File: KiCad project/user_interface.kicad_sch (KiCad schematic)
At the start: 12 parts, among them J4 Conn_01x05, J6 B4B-XH-AM__LF__SN_, Q2 BC817, Q3 BC817, SW1 SMD_6x3.5mm_h2.5mm, SW2 SMD_6x3.5mm_h2.5mm

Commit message: Fixed lots of bugs.
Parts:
- removed R36: 10K, Resistor_SMD:R_0201_0603Metric, symbol Device:R
- C21: footprint SparkFun-Capacitor:C_0603_1608Metric -> Capacitor_SMD:C_0805_2012Metric
- C22: value 0.1u -> 1u; footprint SparkFun-Capacitor:C_0603_1608Metric -> Capacitor_SMD:C_0805_2012Metric; Purpose Debounce capacitor -> (none)
- J5: renamed from J6; footprint B4B-XH-AM__LF__SN_:JST_B4B-XH-AM__LF__SN_ -> Project_Library:JST_B4B-XH-AM__LF__SN_
- J6: renamed from J4; footprint (none) -> Connector_PinHeader_2.54mm:PinHeader_1x05_P2.54mm_Vertical
- R32: renamed from R37; footprint Resistor_SMD:R_0201_0603Metric -> Resistor_SMD:R_0805_2012Metric
- R33: renamed from R13; footprint Resistor_SMD:R_0201_0603Metric -> Resistor_SMD:R_0805_2012Metric
- R34: renamed from R38; footprint Resistor_SMD:R_0201_0603Metric -> Resistor_SMD:R_0805_2012Metric
- SW1, SW2: footprint SparkFun-Switch:Push_SMD_6x3.5mm -> Button_Switch_THT:SW_PUSH_6mm

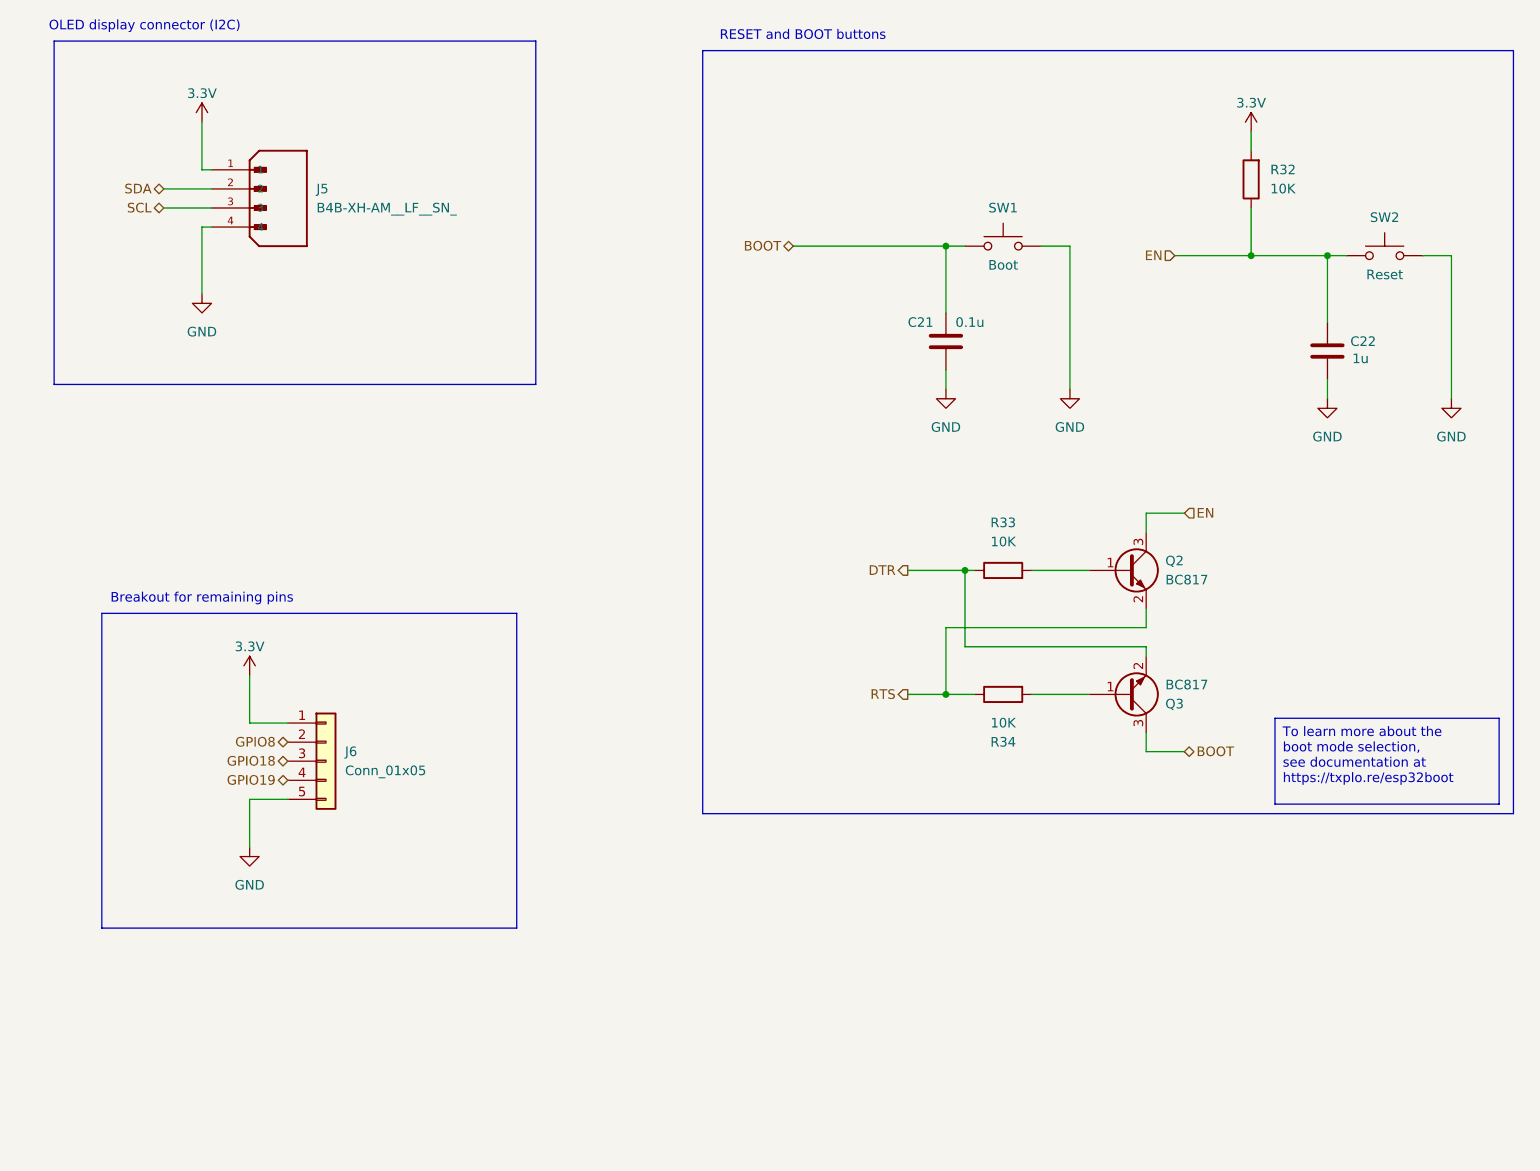
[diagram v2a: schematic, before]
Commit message: Replaced the button, USB, bat connector with new symbols and footprints. Completed draft layout and routing.
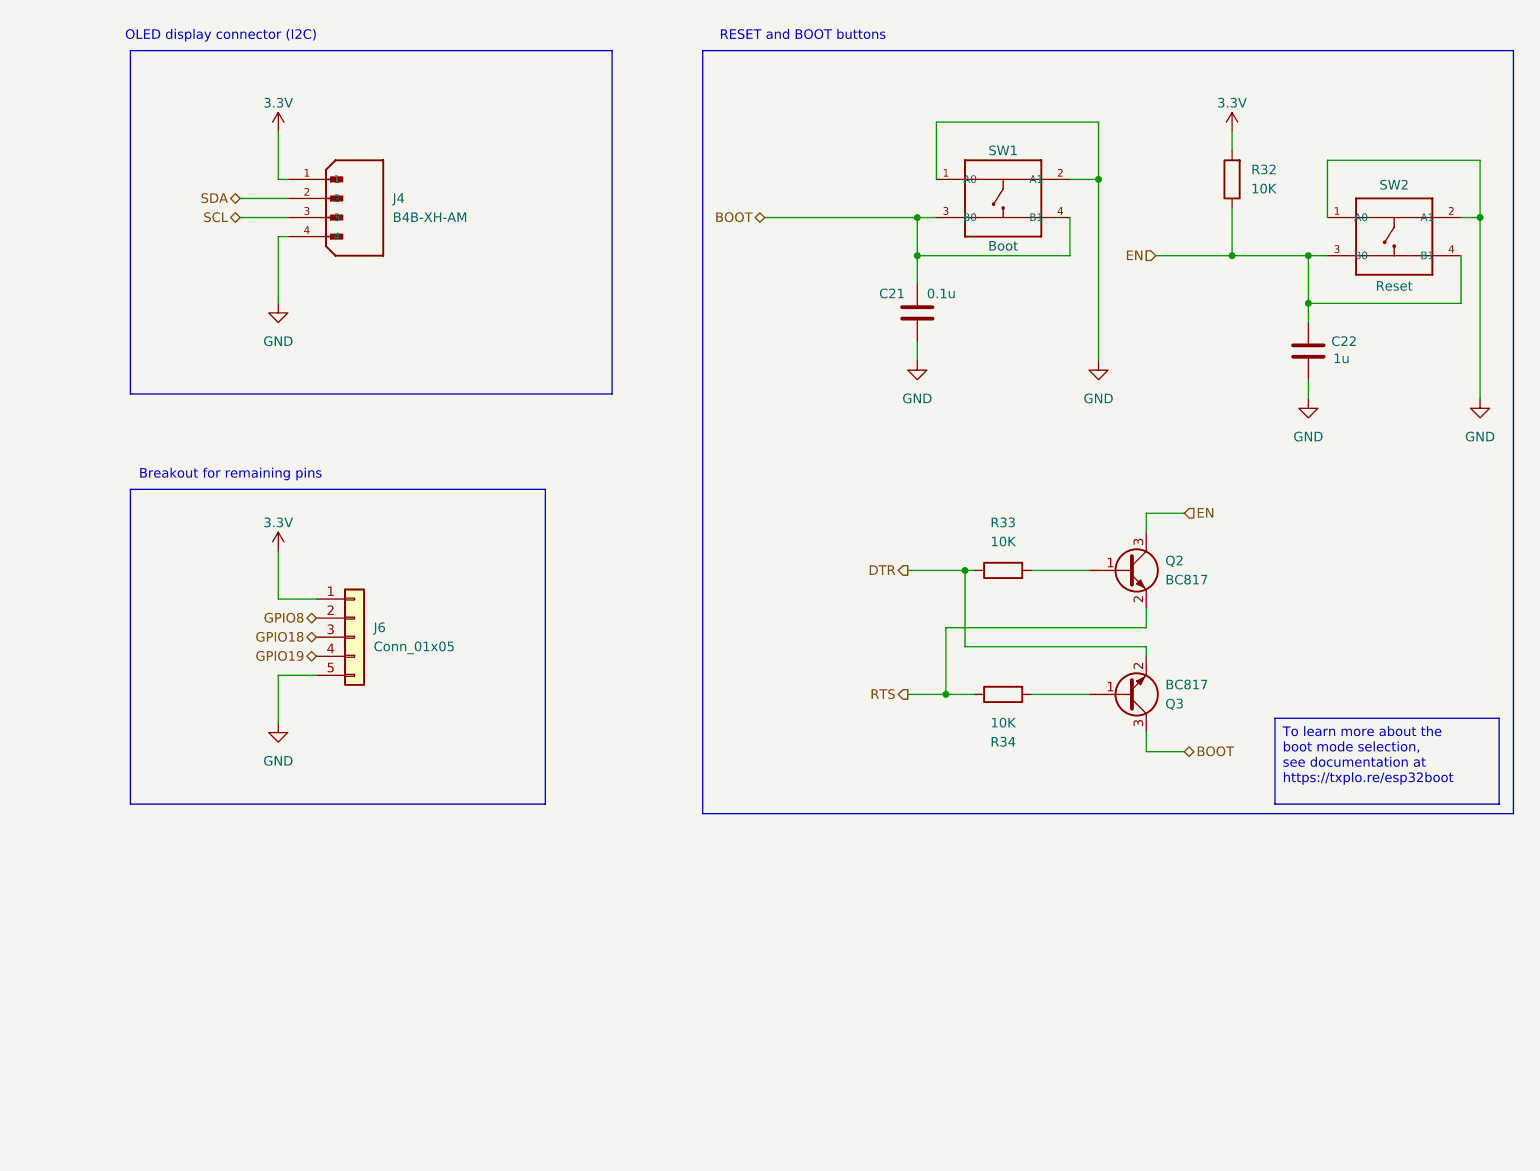
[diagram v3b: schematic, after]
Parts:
- J4: renamed from J5; value B4B-XH-AM__LF__SN_ -> B4B-XH-AM; Manufacturer_Part_Number (none) -> B4B-XH-AM
- Q2, Q3: Manufacturer_Part_Number (none) -> BC817; PACKAGE (none) -> SOT-23
- R32, R33, R34: PACKAGE (none) -> 0805
- SW1, SW2: value SMD_6x3.5mm_h2.5mm -> 1101NE; footprint Button_Switch_THT:SW_PUSH_6mm -> Footprints:SW4-SMD-5.2X5.2X1.5MM; symbol SparkFun-Switch:SPST_Push_SMD_6x3.5mm_h2.5mm -> SMD-BUTTON_4P-5.2X5.2X1.5MM-SKQGADE010_:SMD-BUTTON_4P-5.2X5.2X1.5MM-SKQGADE010_; Availability (none) -> In Stock; Check_prices (none) -> https://www.snapeda.com/parts/SKQGADE010/ALPS/view-part/?re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; Description_1 (none) -> Switch Tactile N.O. SPST Round Button Gull Wing 0.05A 12VDC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; MF (none) -> ALPS; MP (none) -> SKQGADE010; Manufacturer_Part_Number (none) -> 1101NE; Package (none) -> SMD-4 ALPS; Price (none) -> None; SnapEDA_Link (none) -> https://www.snapeda.com/parts/SKQGADE010/ALPS/view-part/?re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
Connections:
- net BOOT: now also SW1.3 (B0), SW1.4 (B1); no longer SW1.1
- net EN: now also SW2.3 (B0), SW2.4 (B1); no longer SW2.1
- net GND: now also SW1.1 (A0), SW2.1 (A0)
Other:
- moved on the sheet: C21, C22, J4, J6, R32

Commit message: Completed draft of the layout.
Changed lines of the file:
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@@
+	)
+	(symbol
+		(lib_id "Graphic:Logo_Open_Hardware_Small")
+		(at 52.07 185.42 0)
+		(unit 1)
+		(exclude_from_sim yes)
+		(in_bom no)
+		(on_board yes)
+		(dnp no)
+		(fields_autoplaced yes)
+		(property "Reference" "#SYM3"
+			(at 52.07 178.435 0)
+			(effects
+				(font
+					(size 1.27 1.27)
+				)
+				(hide yes)
+			)
+		)
+		(property "Value" "Logo_Open_Hardware_Small"
+			(at 52.07 191.135 0)
+			(effects
+				(font
+					(size 1.27 1.27)
+				)
+				(hide yes)
+			)
+		)
+		(property "Footprint" "Footprints:TE_Logo_11.6x4"
+			(at 52.07 185.42 0)
+			(effects
+				(font
+					(size 1.27 1.27)
+				)
+				(hide yes)
+			)
+		)
+		(property "Datasheet" "~"
+			(at 52.07 185.42 0)
+			(effects
+				(font
+					(size 1.27 1.27)
+				)
+				(hide yes)
+			)
+		)
+		(property "Description" "Open Hardware logo, small"
+			(at 52.07 185.42 0)
+			(effects
+				(font
+					(size 1.27 1.27)
+				)
+				(hide yes)
+			)
+		)
+		(property "Comments" ""
+			(at 52.07 185.42 0)
+			(effects
+				(font
+					(size 1.27 1.27)
+				)
+				(hide yes)
+			)
+		)
+		(instances
+			(project "ESP32 sensor board"
+				(path "/16c571a0-8550-4f05-972c-22b0701cbf02/09ec4a32-ddff-43cd-8e21-9ef822101853/9638f799-907f-4116-a2c8-fb3f1731f620"
+					(reference "#SYM3")
+					(unit 1)
+				)
+			)
+		)
 	)
 	(symbol
@@
 	)
 	(symbol
+		(lib_id "Graphic:Logo_Open_Hardware_Small")
+		(at 52.07 171.45 0)
+		(unit 1)
+		(exclude_from_sim yes)
+		(in_bom no)
+		(on_board yes)
+		(dnp no)
+		(fields_autoplaced yes)
+		(property "Reference" "#SYM2"
+			(at 52.07 164.465 0)
+			(effects
+				(font
+					(size 1.27 1.27)
+				)
+				(hide yes)
+			)
+		)
+		(property "Value" "Logo_Open_Hardware_Small"
+			(at 52.07 177.165 0)
+			(effects
+				(font
+					(size 1.27 1.27)
+				)
+				(hide yes)
+			)
+		)
+		(property "Footprint" "Symbol:KiCad-Logo_5mm_SilkScreen"
+			(at 52.07 171.45 0)
+			(effects
+				(font
+					(size 1.27 1.27)
+				)
+				(hide yes)
+			)
+		)
+		(property "Datasheet" "~"
+			(at 52.07 171.45 0)
+			(effects
+				(font
+					(size 1.27 1.27)
+				)
+				(hide yes)
+			)
+		)
+		(property "Description" "Open Hardware logo, small"
+			(at 52.07 171.45 0)
+			(effects
+				(font
+					(size 1.27 1.27)
+				)
+				(hide yes)
+			)
+		)
+		(property "Comments" ""
+			(at 52.07 171.45 0)
+			(effects
+				(font
+					(size 1.27 1.27)
+				)
+				(hide yes)
+			)
+		)
+		(instances
+			(project "ESP32 sensor board"
+				(path "/16c571a0-8550-4f05-972c-22b0701cbf02/09ec4a32-ddff-43cd-8e21-9ef822101853/9638f799-907f-4116-a2c8-fb3f1731f620"
+					(reference "#SYM2")
+					(unit 1)
+				)
+			)
+		)
+	)
+	(symbol
 		(lib_id "Transistor_BJT:BC817")
 		(at 179.07 128.27 0)
@@
 					(unit 1)
 				)
+			)
+		)
+	)
+	(symbol
+		(lib_id "Graphic:Logo_Open_Hardware_Small")
+		(at 52.07 157.48 0)
+		(unit 1)
+		(exclude_from_sim no)
+		(in_bom no)
+		(on_board yes)
+		(dnp no)
+		(fields_autoplaced yes)
+		(property "Reference" "#SYM1"
+			(at 52.07 150.495 0)
+			(effects
+				(font
+					(size 1.27 1.27)
+				)
+				(hide yes)
+			)
+		)
+		(property "Value" "Logo_Open_Hardware_Small"
+			(at 52.07 163.195 0)
+			(effects
+				(font
+					(size 1.27 1.27)
+				)
+				(hide yes)
+			)
+		)
+		(property "Footprint" "Symbol:OSHW-Logo_5.7x6mm_SilkScreen"
+			(at 52.07 157.48 0)
+			(effects
+				(font
+					(size 1.27 1.27)
+				)
+				(hide yes)
+			)
+		)
+		(property "Datasheet" "~"
+			(at 52.07 157.48 0)
+			(effects
+				(font
+					(size 1.27 1.27)
+				)
+				(hide yes)
+			)
+		)
+		(property "Description" "Open Hardware logo, small"
+			(at 52.07 157.48 0)
+			(effects
+				(font
+					(size 1.27 1.27)
+				)
+				(hide yes)
+			)
+		)
+		(property "Sim.Enable" "0"
+			(at 52.07 157.48 0)
+			(effects
+				(font
+					(size 1.27 1.27)
+				)
+				(hide yes)
+			)
+		)
+		(property "Comments" ""
+			(at 52.07 157.48 0)
+			(effects
+				(font
+					(size 1.27 1.27)
+				)
+				(hide yes)
+			)
+		)
+		(instances
+			(project ""
+				(path "/16c571a0-8550-4f05-972c-22b0701cbf02/09ec4a32-ddff-43cd-8e21-9ef822101853/9638f799-907f-4116-a2c8-fb3f1731f620"
+					(reference "#SYM1")
+					(unit 1)
+				)

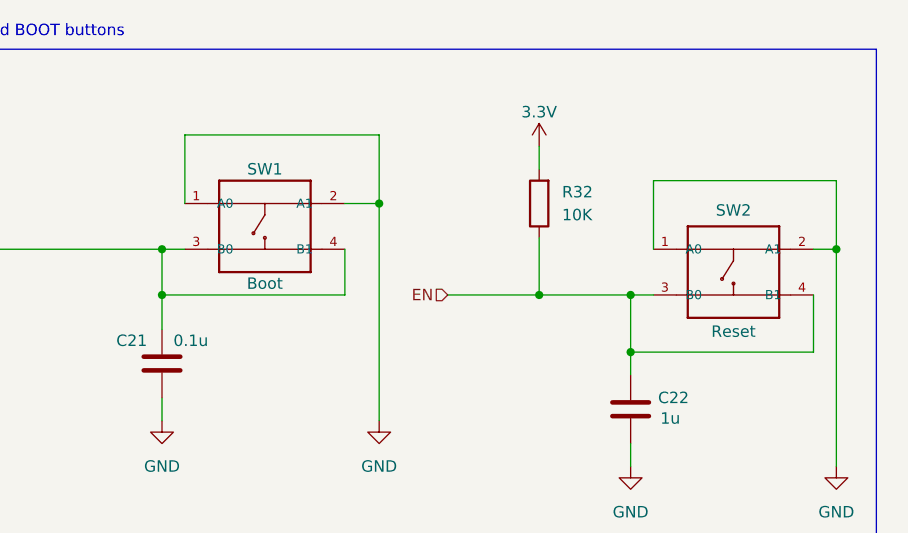
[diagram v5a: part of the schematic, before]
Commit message: Introduced new parts that can be purchased for manufacturing by NextPCB. Corrected numerous issues.
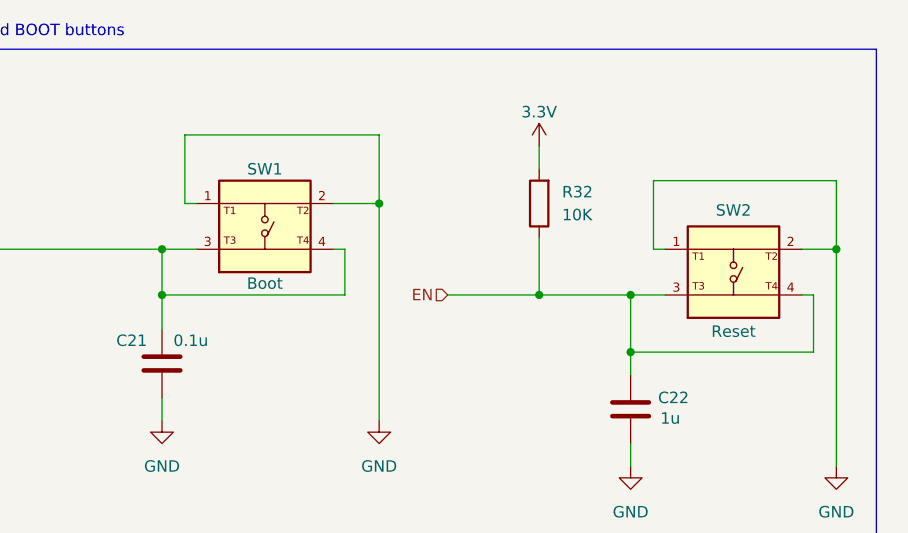
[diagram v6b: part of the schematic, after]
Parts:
- SW1, SW2: footprint Footprints:SW4-SMD-5.2X5.2X1.5MM -> Footprints:SW_USLPT2819DT2TR; symbol SMD-BUTTON_4P-5.2X5.2X1.5MM-SKQGADE010_:SMD-BUTTON_4P-5.2X5.2X1.5MM-SKQGADE010_ -> USLPT2819DT2TR:USLPT2819DT2TR; Check_prices https://www.snapeda.com/parts/SKQGADE010/ALPS/view-part/?re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 -> https://www.snapeda.com/parts/USLPT2819DT2TR/TE+Connectivit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; Description_1 Switch Tactile N.O. SPST Round Button Gull Wing 0.05A 12VDC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 -> Tactile Switch SPST-NO Top Actuated Surface Mount; MANUFACTURER (none) -> TE CONNECTIVITY; MF ALPS -> TE Connectivity; MP SKQGADE010 -> USLPT2819DT2TR; PARTREV (none) -> P; Package SMD-4 ALPS -> None; STANDARD (none) -> Manufacturer Recommendations; SnapEDA_Link https://www.snapeda.com/parts/SKQGADE010/ALPS/view-part/?re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 -> https://www.snapeda.com/parts/USLPT2819DT2TR/TE+Connectivit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
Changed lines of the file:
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@@
 	(wire
 		(pts
+			(xy 170.18 64.77) (xy 171.45 64.77)
+		)
+		(stroke
+			(width 0)
+			(type default)
+		)
+	)
+	(wire
+		(pts
 			(xy 171.45 69.85) (xy 151.13 69.85)
 		)
@@
 	(wire
 		(pts
+			(xy 222.25 64.77) (xy 226.06 64.77)
+		)
+		(stroke
+			(width 0)
+			(type default)
+		)
+	)
+	(wire
+		(pts
 			(xy 181.61 135.89) (xy 186.69 135.89)
 		)
@@
 	(wire
 		(pts
-			(xy 153.67 64.77) (xy 151.13 64.77)
+			(xy 151.13 64.77) (xy 154.94 64.77)
 		)
 		(stroke
@@
 	(wire
 		(pts
-			(xy 175.26 59.69) (xy 171.45 59.69)
-		)
-		(stroke
-			(width 0)
-			(type default)
-		)
-	)
-	(wire
-		(pts
 			(xy 223.52 69.85) (xy 223.52 76.2)
 		)
@@
 	(wire
 		(pts
+			(xy 170.18 59.69) (xy 175.26 59.69)
+		)
+		(stroke
+			(width 0)
+			(type default)
+		)
+	)
+	(wire
+		(pts
 			(xy 181.61 121.92) (xy 157.48 121.92)
 		)
@@
 	(wire
 		(pts
-			(xy 205.74 69.85) (xy 203.2 69.85)
+			(xy 203.2 69.85) (xy 207.01 69.85)
 		)
 		(stroke
@@
 	(wire
 		(pts
-			(xy 226.06 64.77) (xy 223.52 64.77)
+			(xy 153.67 59.69) (xy 154.94 59.69)
 		)
 		(stroke
@@
 	(wire
 		(pts
+			(xy 205.74 64.77) (xy 207.01 64.77)
+		)
+		(stroke
+			(width 0)
+			(type default)
+		)
+	)
+	(wire
+		(pts
 			(xy 66.04 125.73) (xy 66.04 132.08)
 		)
@@
 	(wire
 		(pts
+			(xy 222.25 69.85) (xy 223.52 69.85)
+		)
+		(stroke
+			(width 0)
+			(type default)
+		)
+	)
+	(wire
+		(pts
 			(xy 193.04 53.34) (xy 193.04 55.88)
 		)
@@
 	)
 	(symbol
-		(lib_id "SMD-BUTTON_4P-5.2X5.2X1.5MM-SKQGADE010_:SMD-BUTTON_4P-5.2X5.2X1.5MM-SKQGADE010_")
+		(lib_id "USLPT2819DT2TR:USLPT2819DT2TR")
 		(at 214.63 67.31 0)
 		(unit 1)
@@
 			)
 		)
-		(property "Footprint" "Footprints:SW4-SMD-5.2X5.2X1.5MM"
+		(property "Footprint" "Footprints:SW_USLPT2819DT2TR"
 			(at 214.63 67.31 0)
 			(effects
@@
 			)
 		)
-		(property "MF" "ALPS"
+		(property "MF" "TE Connectivity"
 			(at 214.63 67.31 0)
 			(effects
@@
 			)
 		)
-		(property "Description_1" "\n                        \n                            Switch Tactile N.O. SPST Round Button Gull Wing 0.05A 12VDC 2.55N SMD T/R\n                        \n"
+		(property "Description_1" "\n                        \n                            Tactile Switch SPST-NO Top Actuated Surface Mount\n                        \n"
 			(at 214.63 67.31 0)
 			(effects
@@
 			)
 		)
-		(property "Package" "SMD-4 ALPS"
+		(property "Package" "None"
 			(at 214.63 67.31 0)
 			(effects
@@
 			)
 		)
-		(property "SnapEDA_Link" "https://www.snapeda.com/parts/SKQGADE010/ALPS/view-part/?ref=snap"
+		(property "SnapEDA_Link" "https://www.snapeda.com/parts/USLPT2819DT2TR/TE+Connectivity+ALCOSWITCH+Switches/view-part/?ref=snap"
 			(at 214.63 67.31 0)
 			(effects
@@
 			)
 		)
-		(property "MP" "SKQGADE010"
+		(property "MP" "USLPT2819DT2TR"
 			(at 214.63 67.31 0)
 			(effects
@@
 			)
 		)
-		(property "Check_prices" "https://www.snapeda.com/parts/SKQGADE010/ALPS/view-part/?ref=eda"
+		(property "Check_prices" "https://www.snapeda.com/parts/USLPT2819DT2TR/TE+Connectivity+ALCOSWITCH+Switches/view-part/?ref=eda"
+			(at 214.63 67.31 0)
+			(effects
+				(font
+					(size 1.27 1.27)
+				)
+				(justify bottom)
+				(hide yes)
+			)
+		)
+		(property "STANDARD" "Manufacturer Recommendations"
+			(at 214.63 67.31 0)
+			(effects
+				(font
+					(size 1.27 1.27)
+				)
+				(justify bottom)
+				(hide yes)
+			)
+		)
+		(property "PARTREV" "P"
+			(at 214.63 67.31 0)
+			(effects
+				(font
+					(size 1.27 1.27)
+				)
+				(justify bottom)
+				(hide yes)
+			)
+		)
+		(property "MANUFACTURER" "TE CONNECTIVITY"
 			(at 214.63 67.31 0)
 			(effects
@@
 			)
 		)
+		(property "Comments" ""
+			(at 214.63 67.31 0)
+			(effects
+				(font
+					(size 1.27 1.27)
+				)
+				(hide yes)
+			)
+		)
 		(pin "2"
 		)
@@
 	)
 	(symbol
-		(lib_id "SMD-BUTTON_4P-5.2X5.2X1.5MM-SKQGADE010_:SMD-BUTTON_4P-5.2X5.2X1.5MM-SKQGADE010_")
+		(lib_id "USLPT2819DT2TR:USLPT2819DT2TR")
 		(at 162.56 62.23 0)
 		(unit 1)
@@
 			)
 		)
-		(property "Footprint" "Footprints:SW4-SMD-5.2X5.2X1.5MM"
+		(property "Footprint" "Footprints:SW_USLPT2819DT2TR"
 			(at 162.56 62.23 0)
 			(effects
@@
 			)
 		)
-		(property "MF" "ALPS"
+		(property "MF" "TE Connectivity"
 			(at 162.56 62.23 0)
 			(effects
@@
 			)
 		)
-		(property "Description_1" "\n                        \n                            Switch Tactile N.O. SPST Round Button Gull Wing 0.05A 12VDC 2.55N SMD T/R\n                        \n"
+		(property "Description_1" "\n                        \n                            Tactile Switch SPST-NO Top Actuated Surface Mount\n                        \n"
 			(at 162.56 62.23 0)
 			(effects
@@
 			)
 		)
-		(property "Package" "SMD-4 ALPS"
+		(property "Package" "None"
 			(at 162.56 62.23 0)
 			(effects
@@
 			)
 		)
-		(property "SnapEDA_Link" "https://www.snapeda.com/parts/SKQGADE010/ALPS/view-part/?ref=snap"
+		(property "SnapEDA_Link" "https://www.snapeda.com/parts/USLPT2819DT2TR/TE+Connectivity+ALCOSWITCH+Switches/view-part/?ref=snap"
 			(at 162.56 62.23 0)
 			(effects
@@
 			)
 		)
-		(property "MP" "SKQGADE010"
+		(property "MP" "USLPT2819DT2TR"
 			(at 162.56 62.23 0)
 			(effects
@@
 			)
 		)
-		(property "Check_prices" "https://www.snapeda.com/parts/SKQGADE010/ALPS/view-part/?ref=eda"
+		(property "Check_prices" "https://www.snapeda.com/parts/USLPT2819DT2TR/TE+Connectivity+ALCOSWITCH+Switches/view-part/?ref=eda"
+			(at 162.56 62.23 0)
+			(effects
+				(font
+					(size 1.27 1.27)
+				)
+				(justify bottom)
+				(hide yes)
+			)
+		)
+		(property "Comments" ""
+			(at 162.56 62.23 0)
+			(effects
+				(font
+					(size 1.27 1.27)
+				)
+				(hide yes)
+			)
+		)
+		(property "STANDARD" "Manufacturer Recommendations"
+			(at 162.56 62.23 0)
+			(effects
+				(font
+					(size 1.27 1.27)
+				)
+				(justify bottom)
+				(hide yes)
+			)
+		)
+		(property "PARTREV" "P"
+			(at 162.56 62.23 0)
+			(effects
+				(font
+					(size 1.27 1.27)
+				)
+				(justify bottom)
+				(hide yes)
+			)
+		)
+		(property "MANUFACTURER" "TE CONNECTIVITY"
 			(at 162.56 62.23 0)
 			(effects
